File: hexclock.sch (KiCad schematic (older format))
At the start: 39 parts, among them J1 USB_B_Micro, U1 ATtiny402-SS, U2 MCP7940N-xSN, Y1 7pF CL

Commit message: v0.0.0 finished
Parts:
- removed U1: ATtiny402-SS, Package_SO:SOIC-8_3.9x4.9mm_P1.27mm, symbol MCU_Microchip_ATtiny:ATtiny402-SS
- added R8: 20kR, Resistor_SMD:R_0805_2012Metric, symbol Device:R_Small
- added U2: ATtiny88-MU, Package_DFN_QFN:QFN-32-1EP_5x5mm_P0.5mm_EP3.1x3.1mm, symbol MCU_Microchip_ATtiny:ATtiny88-MU
- U1: renamed from U2; footprint Package_SO:SOIC-8-1EP_3.9x4.9mm_P1.27mm_EP2.41x3.3mm -> Package_SO:SOIC-8_3.9x4.9mm_P1.27mm
- renumbered C6 to C1, C7 to C2, C1 to C6, C2 to C7, D12 to D10, D15 to D11, D18 to D12, D3 to D13, D7 to D14, D10 to D15, D13 to D16, D16 to D17, D4 to D18, D5 to D2, D8 to D3, D11 to D4, D14 to D5, D17 to D6, D2 to D7, D6 to D8, R3 to R1, R4 to R2, R5 to R3, R6 to R4, R7 to R5, R1 to R6, R2 to R7
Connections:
- net +5V: now also R8.1, U2.18 (AVCC), U2.4 (VCC)
- net DOUT: now also U2.23 (PC0)
- net GND: now also C6.2, C7.2, U2.1 (PD3), U2.10 (PD6), U2.11 (PD7), U2.12 (PB0), U2.13 (PB1), U2.14 (PB2), U2.15 (PB3), U2.16 (PB4), U2.17 (PB5), U2.19 (PA0), U2.2 (PD4), U2.20 (PC7), U2.21 (GND), U2.22 (PA1), U2.26 (PC3), U2.3 (PA2), U2.30 (PD0), U2.31 (PD1), U2.33 (GND), U2.5 (GND), U2.6 (PA3), U2.7 (PB6), U2.8 (PB7), U2.9 (PD5)
- net HH: now also U2.24 (PC1)
- net MM: now also U2.25 (PC2)
- net SCL: now also U2.28 (PC5)
- net SDA: now also U2.27 (PC4)
- net SINT: now reaches U1.7 (MFP)
- net SINT: now also R8.2, U2.32 (PD2)
- net at R6.2, S2.2: no longer C6.2, C7.2
- net at R1.2: now also U2.29 (~RESET~/PC6)
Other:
- moved on the sheet: BT1, C1, C2, C3, C4, C5, C6, C7, D1, D10, D11, D12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

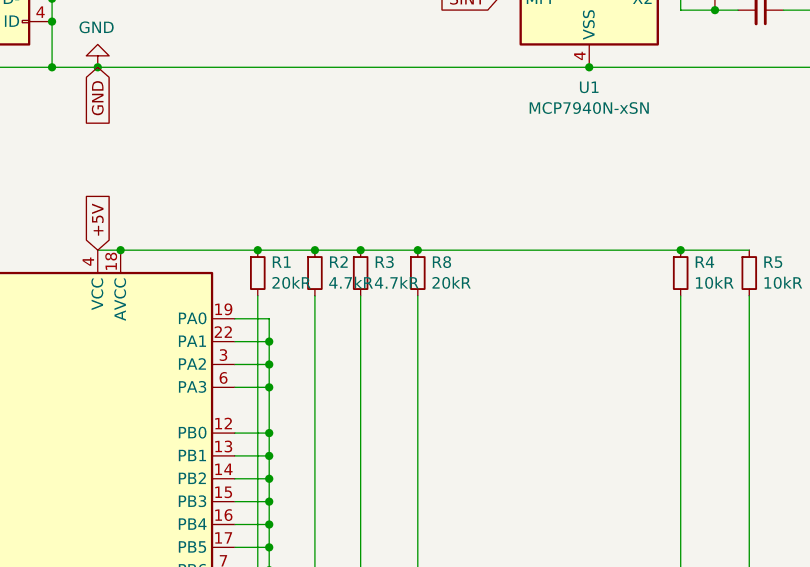
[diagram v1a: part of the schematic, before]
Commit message: Fix i2c pullups
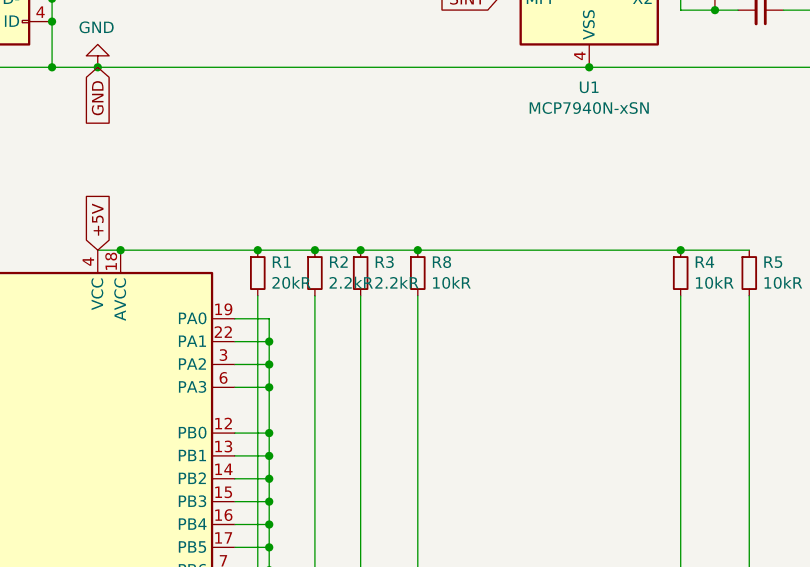
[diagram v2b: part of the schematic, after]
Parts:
- R2, R3: value 4.7kR -> 2.2kR
- R8: value 20kR -> 10kR
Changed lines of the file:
@@
 P 3150 3100
 F 0 "R8" H 3209 3146 50  0000 L CNN
-F 1 "20kR" H 3209 3055 50  0000 L CNN
+F 1 "10kR" H 3209 3055 50  0000 L CNN
 F 2 "Resistor_SMD:R_0805_2012Metric" H 3150 3100 50  0001 C CNN
 F 3 "~" H 3150 3100 50  0001 C CNN
@@
 P 2900 3100
 F 0 "R3" H 2959 3146 50  0000 L CNN
-F 1 "4.7kR" H 2959 3055 50  0000 L CNN
+F 1 "2.2kR" H 2959 3055 50  0000 L CNN
 F 2 "Resistor_SMD:R_0805_2012Metric" H 2900 3100 50  0001 C CNN
 F 3 "~" H 2900 3100 50  0001 C CNN
@@
 P 2700 3100
 F 0 "R2" H 2759 3146 50  0000 L CNN
-F 1 "4.7kR" H 2759 3055 50  0000 L CNN
+F 1 "2.2kR" H 2759 3055 50  0000 L CNN
 F 2 "Resistor_SMD:R_0805_2012Metric" H 2700 3100 50  0001 C CNN
 F 3 "~" H 2700 3100 50  0001 C CNN

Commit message: Switch to using oscillator; update version
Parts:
- removed BT1: Battery_Cell, Battery:BatteryHolder_Keystone_3034_1x20mm, symbol Device:Battery_Cell
- removed C1, C2: 8pF, Capacitor_SMD:C_0805_2012Metric, symbol Device:C_Small
- removed U1: MCP7940N-xSN, Package_SO:SOIC-8_3.9x4.9mm_P1.27mm, symbol Timer:MCP7940N-xSN
- removed Y1: 7pF CL, Crystal:Crystal_SMD_3215-2Pin_3.2x1.5mm, symbol Device:Crystal
- added J2: AVR-ISP-6, Connector_PinHeader_2.54mm:PinHeader_2x03_P2.54mm_Vertical_SMD, symbol Connector:AVR-ISP-6
- added Q1: BSS138-7-F, digikey-footprints:SOT-23-3, symbol dk_Transistors-FETs-MOSFETs-Single:BSS138-7-F
- added U1: MCP1700T-3302E_TT, digikey-footprints:SOT-23-3, symbol dk_PMIC-Voltage-Regulators-Linear:MCP1700T-3302E_TT
- added X1: ECS-327TXO, Oscillator:ECS-327MVATX-3, symbol Oscillator:ECS-327TXO
- R2, R3: value 2.2kR -> 10kR
- U2: footprint Package_DFN_QFN:QFN-32-1EP_5x5mm_P0.5mm_EP3.1x3.1mm -> Package_QFP:TQFP-32_7x7mm_P0.8mm; symbol MCU_Microchip_ATtiny:ATtiny88-MU -> MCU_Microchip_ATtiny:ATtiny88-AU
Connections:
- net +5V: now also J2.2 (VCC), U1.3 (IN); no longer R2.1, R8.1
- net GND: now also U2.27 (PC4), U2.28 (PC5), J2.6 (GND), U1.1 (GND), X1.2 (GND); no longer U2.15 (PB3), U2.16 (PB4), U2.17 (PB5), U2.33 (GND)
- net SINT: now also R3.2, Q1.3 (D); no longer R8.2
- net RST: now reaches R1.2, U2.29 (~RESET~/PC6)
- net RST: now also J2.5 (~RST)
- removed net SCL: R3.2, U2.28 (PC5)
- net SDA: no longer names the net of R2.2
- net SDA: now also X1.1 (OE); no longer U2.27 (PC4)
- new net +3.3V: Q1.1 (G), R2.1, R8.1, U1.2 (OUT), X1.4 (VDD)
- new net MISO: J2.1 (MISO), U2.16 (PB4)
- new net MOSI: J2.4 (MOSI), U2.15 (PB3)
- new net SCK: J2.3 (SCK), U2.17 (PB5)
- new net USIT: Q1.2 (S), R8.2, X1.3 (OUT)

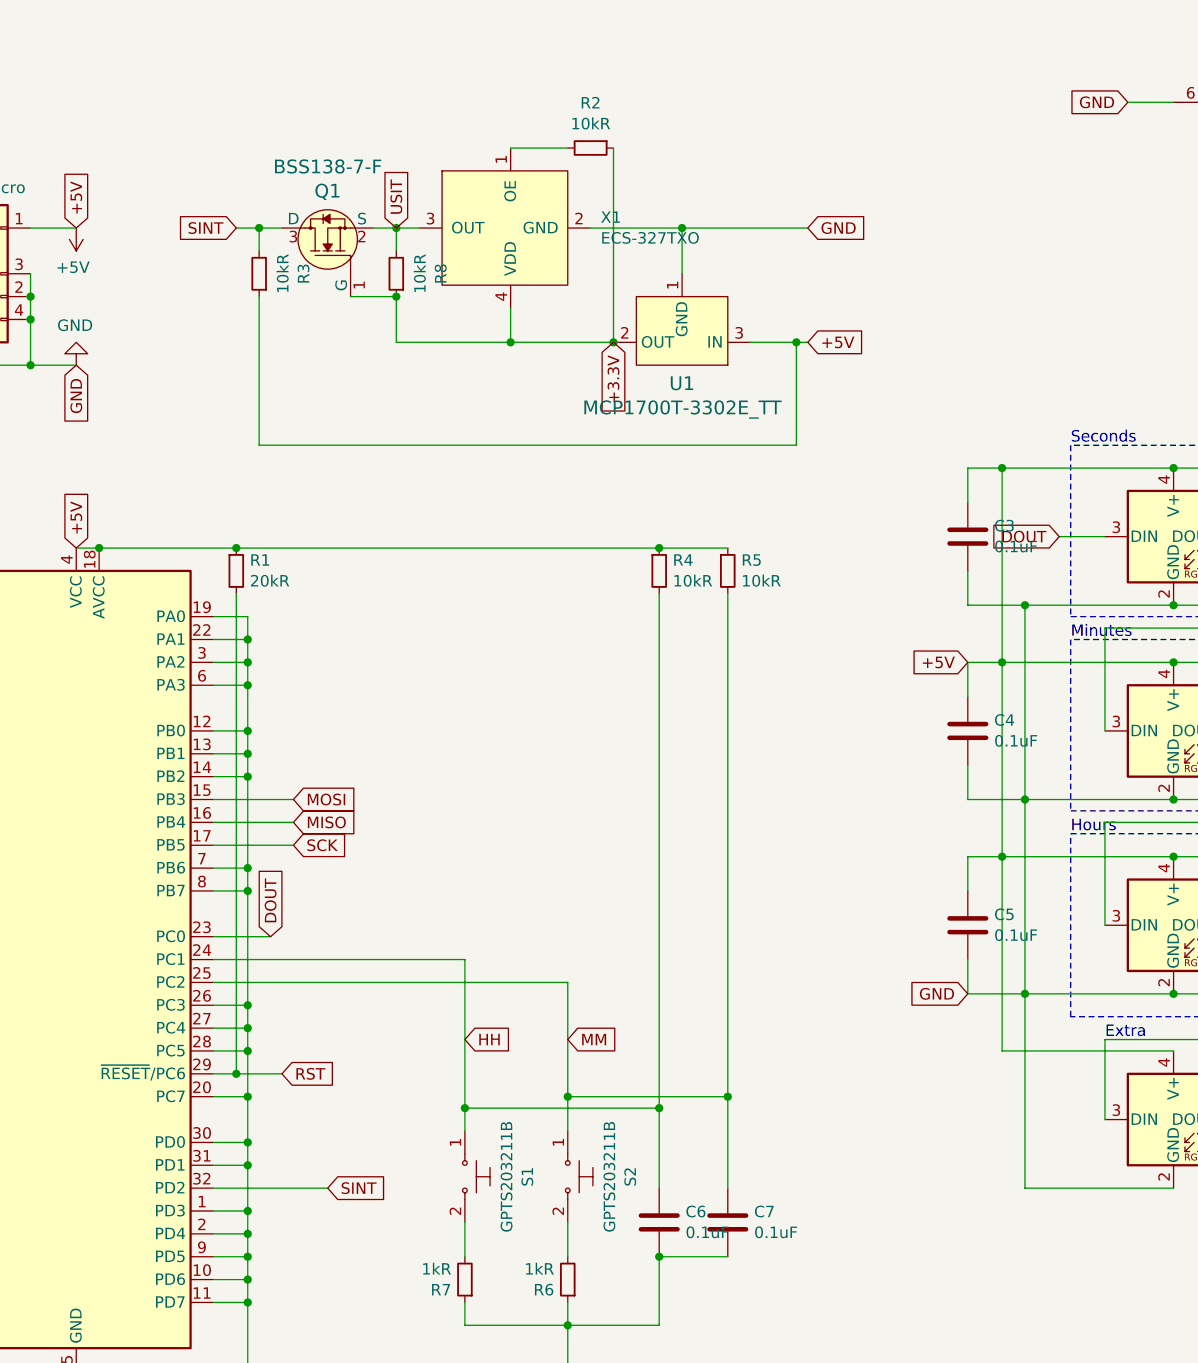
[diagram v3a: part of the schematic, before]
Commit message: Change time mech to RTC
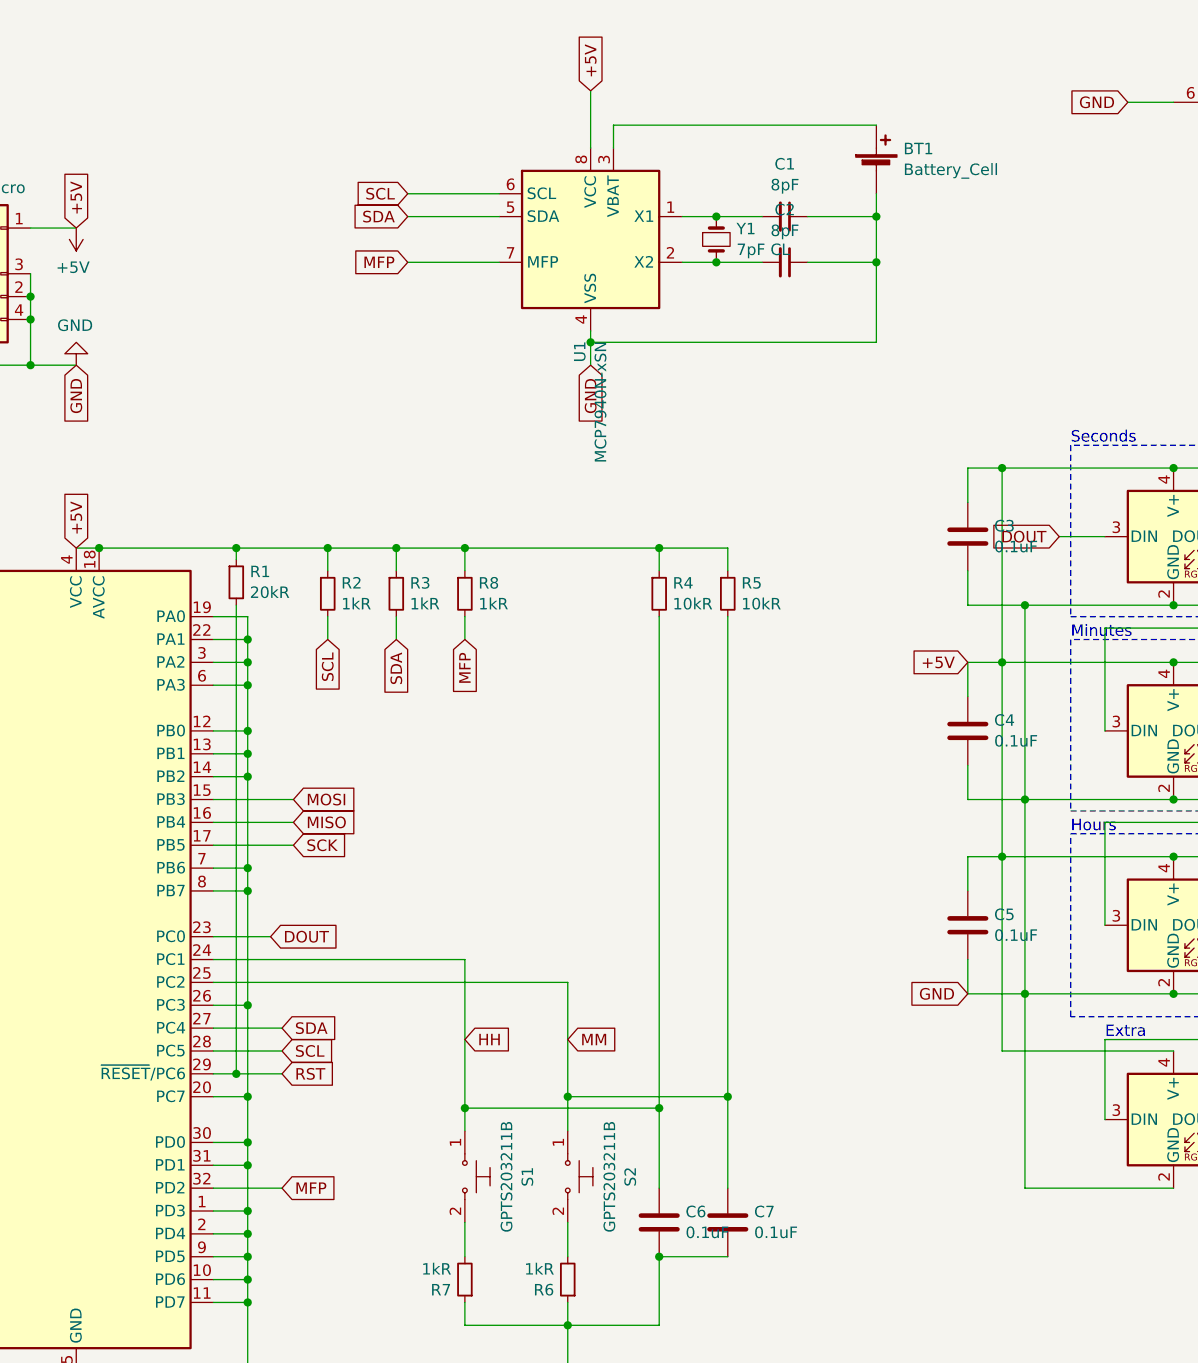
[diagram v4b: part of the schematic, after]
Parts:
- removed Q1: BSS138-7-F, digikey-footprints:SOT-23-3, symbol dk_Transistors-FETs-MOSFETs-Single:BSS138-7-F
- removed U1: MCP1700T-3302E_TT, digikey-footprints:SOT-23-3, symbol dk_PMIC-Voltage-Regulators-Linear:MCP1700T-3302E_TT
- removed X1: ECS-327TXO, Oscillator:ECS-327MVATX-3, symbol Oscillator:ECS-327TXO
- added BT1: Battery_Cell, Battery:BatteryHolder_Keystone_3034_1x20mm, symbol Device:Battery_Cell
- added C1, C2: 8pF, Capacitor_SMD:C_0805_2012Metric, symbol Device:C_Small
- added U1: MCP7940N-xSN, Package_SO:SOIC-8_3.9x4.9mm_P1.27mm, symbol Timer:MCP7940N-xSN
- added Y1: 7pF CL, Crystal:Crystal_SMD_3215-2Pin_3.2x1.5mm, symbol Device:Crystal_Small
- R2, R3, R8: value 10kR -> 1kR
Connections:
- net +3.3V is gone; now on net +5V: R2.1, R8.1
- net USIT is gone; now on net MFP: R8.2
- net +5V: now also U1.8 (VCC)
- net GND: now also BT1.2 (-), C1.1, C2.1, U1.4 (VSS); no longer U2.27 (PC4), U2.28 (PC5)
- net SCL: now reaches R2.2
- net SCL: now also U2.28 (PC5), U1.6 (SCL)
- net SINT renamed MFP
- net MFP: now also U1.7 (MFP); no longer R3.2
- new net: C1.2, U1.1 (X1), Y1.1
- new net: C2.2, U1.2 (X2), Y1.2
- new net: BT1.1 (+), U1.3 (VBAT)
- new net SDA: R3.2, U1.5 (SDA), U2.27 (PC4)
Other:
- moved on the sheet: R1, R4, R5
